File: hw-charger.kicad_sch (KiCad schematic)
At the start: 34 parts, among them J10 Screw_Terminal_01x02, J17 Conn_01x02, J19 Conn_01x02, J27 Conn_01x05, J3 Screw_Terminal_01x03, J56 Screw_Terminal_01x02, J57 Conn_01x02, J58 Screw_Terminal_01x02, J59 Conn_01x02, J60 Screw_Terminal_01x02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

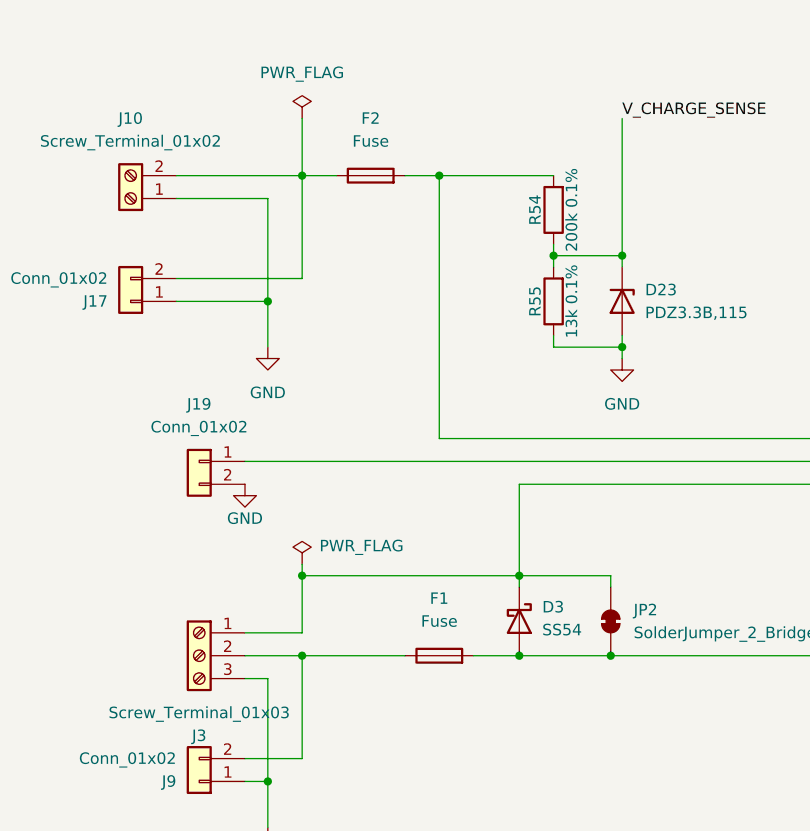
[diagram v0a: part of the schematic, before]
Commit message: Add FT rotations and kibot filter and set fuses DNP
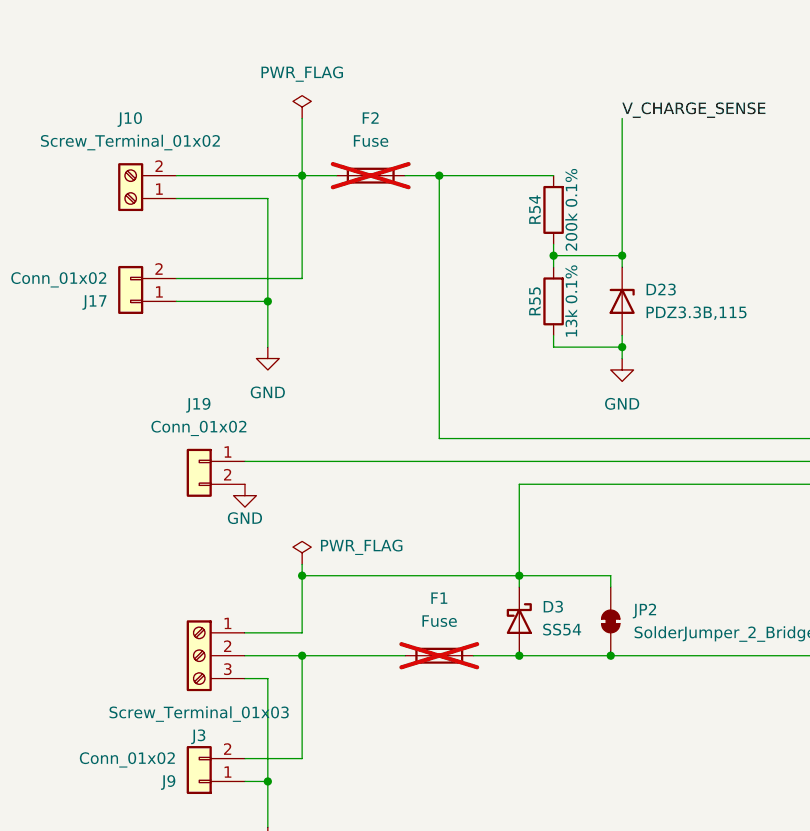
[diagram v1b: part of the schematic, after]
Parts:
- F1, F2: now not fitted
- J19, J27: FT Rotation Offset (none) -> 180
- U14, U15: FT Rotation Offset (none) -> 90
- U16, U17: FT Rotation Offset (none) -> -90
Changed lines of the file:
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@@
 		(in_bom yes)
 		(on_board yes)
-		(dnp no)
+		(dnp yes)
 		(property "Reference" "F1"
 			(at 92.71 139.7 90)
@@
 			)
 		)
-		(property "Height" ""
+		(property "FT Rotation Offset" "180"
 			(at 226.06 66.04 0)
 			(effects
@@
 			)
 		)
-		(property "APPLICATION" ""
+		(property "FT Rotation Offset" "90"
 			(at 261.62 210.82 0)
 			(effects
@@
 			)
 		)
-		(property "Field4" ""
+		(property "FT Rotation Offset" "180"
 			(at 66.04 124.46 0)
 			(effects
@@
 			)
 		)
-		(property "APPLICATION" ""
+		(property "FT Rotation Offset" "90"
 			(at 261.62 201.93 0)
 			(effects
@@
 		(in_bom yes)
 		(on_board yes)
-		(dnp no)
+		(dnp yes)
 		(fields_autoplaced yes)
 		(property "Reference" "F2"
@@
 			)
 		)
-		(property "APPLICATION" ""
+		(property "FT Rotation Offset" "-90"
 			(at 261.62 193.04 0)
 			(effects
@@
 			)
 		)
-		(property "APPLICATION" ""
+		(property "FT Rotation Offset" "-90"
 			(at 261.62 184.15 0)
 			(effects

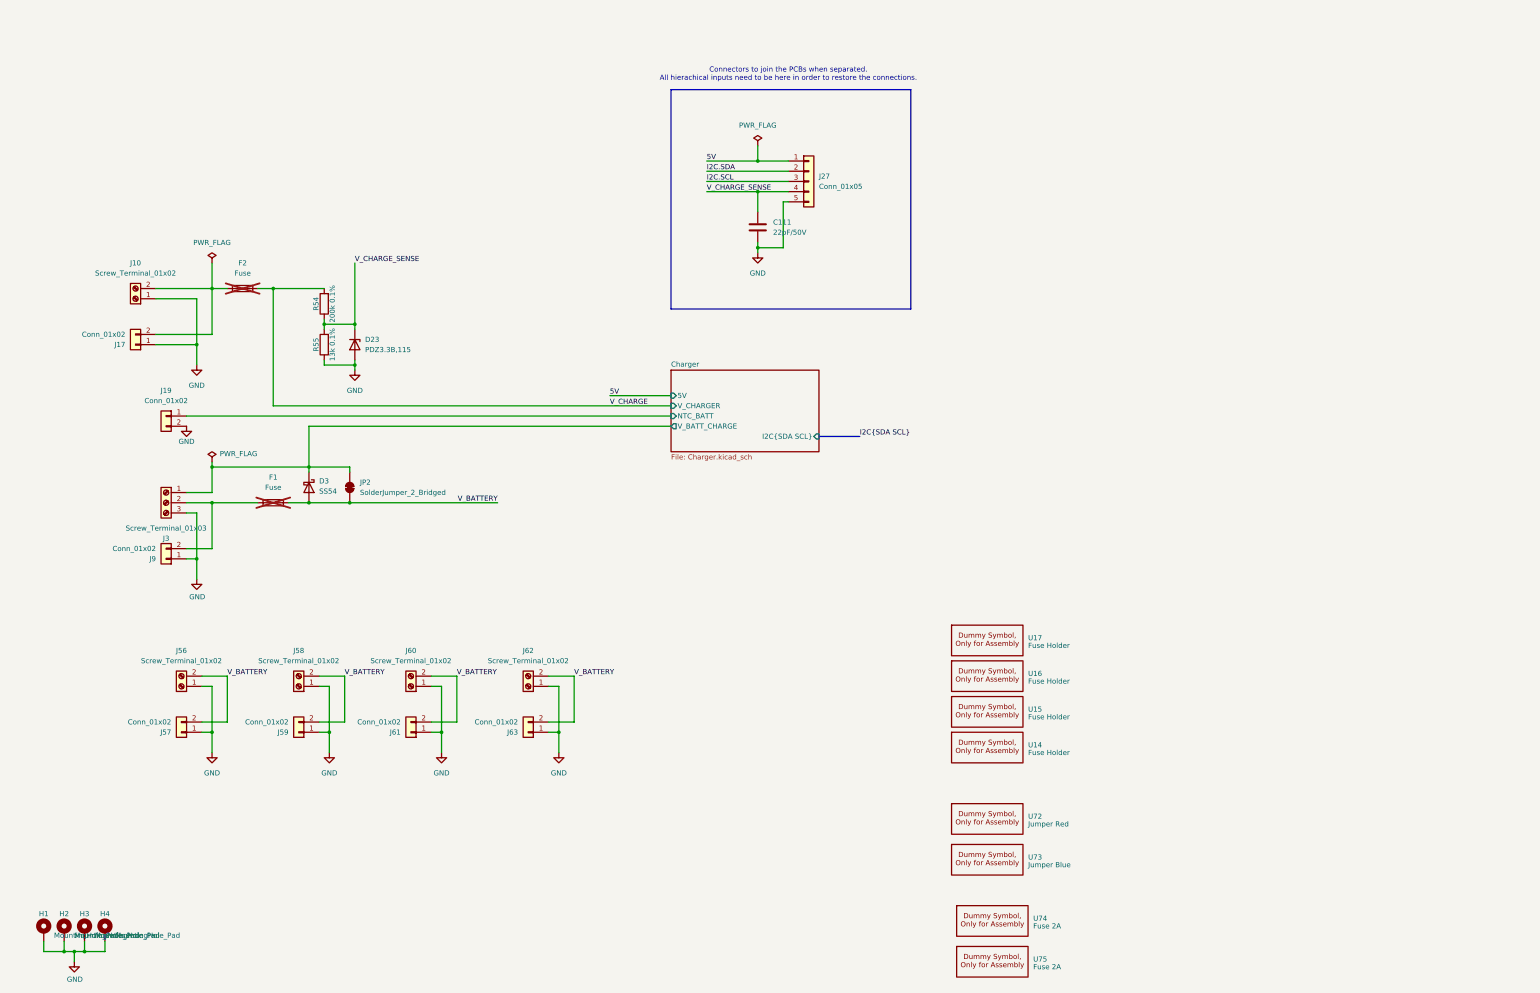
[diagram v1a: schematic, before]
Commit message: Add /CE, NTC Selector, 5V LDO. Fix copper traces, vias in pads and this and that
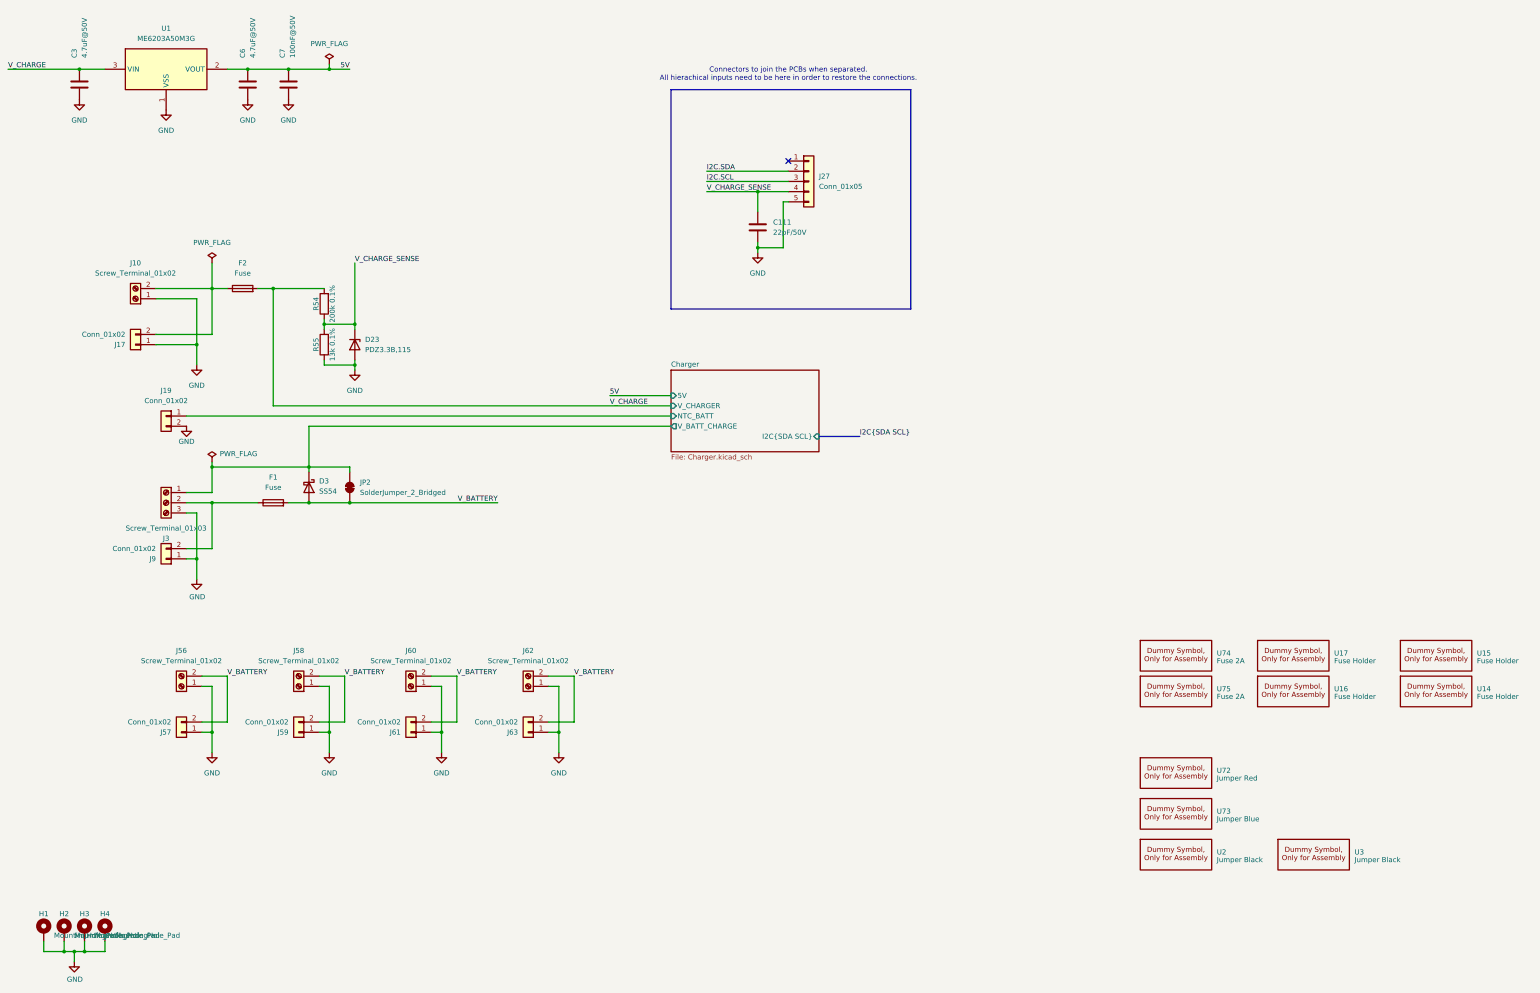
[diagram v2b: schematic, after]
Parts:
- added C3, C6: 4.7uF@50V, Capacitor_SMD:C_1206_3216Metric, symbol Device:C
- added C7: 100nF@50V, Capacitor_SMD:C_0603_1608Metric, symbol Device:C
- added U1: ME6203A50M3G, easyeda2kicad:SOT-23-3_L2.9-W1.6-P1.90-LS2.8-BR, symbol easyeda2kicad:ME6203A50M3G
- added U2, U3: Jumper Black, xtech:SNT-100-BK-H, symbol xtech:Dummy
- F1, F2: footprint local_FUSE:Fuseholder5x20_horiz_open_inline_Type-I -> local_FUSE:Fuseholder5x20_horiz_open_inline_C3130; now fitted
- U72: footprint xtech:Dummy -> xtech:SNT-100-RD-G
- U73: footprint xtech:Dummy -> xtech:SNT-100-BL-H
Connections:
- net 5V: now also C6.1, C7.2, U1.2 (VOUT); no longer J27.1 (Pin_1)
- net GND: now also C3.2, C6.2, C7.1, U1.1 (VSS)
- net V_CHARGE: now also C3.1, U1.3 (VIN)
- no-connect marks 0 -> 1
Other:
- title: OpenMower Charger -> Charger
- moved on the sheet: U14, U15, U16, U17, U72, U73, U74, U75
